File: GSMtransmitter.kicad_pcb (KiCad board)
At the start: 2 copper layers, 69 x 83 mm, 139 parts, among them J1 DS1134-S80BPX, J10 UART1, J11 DG390-5.0-02P, J2 Conn_DEGSON_01x02_Pin, J3 Conn_DEGSON_01x02_Pin, J4 Conn_DEGSON_01x02_Pin, J5 RF Antenna, J6 USB-C, J7 1042240820, J8 1042240820, J9 SWD, Q1 MUN5233DW1, SW1 SM5-180UP-1, U1 AP63203WU, U2 AP63200WU, U3 SIM800C-DS, U4 USBLC6-2SC6, U5 STM32L072CBT6, Y1 4 MHz, Y2 32768 kHz

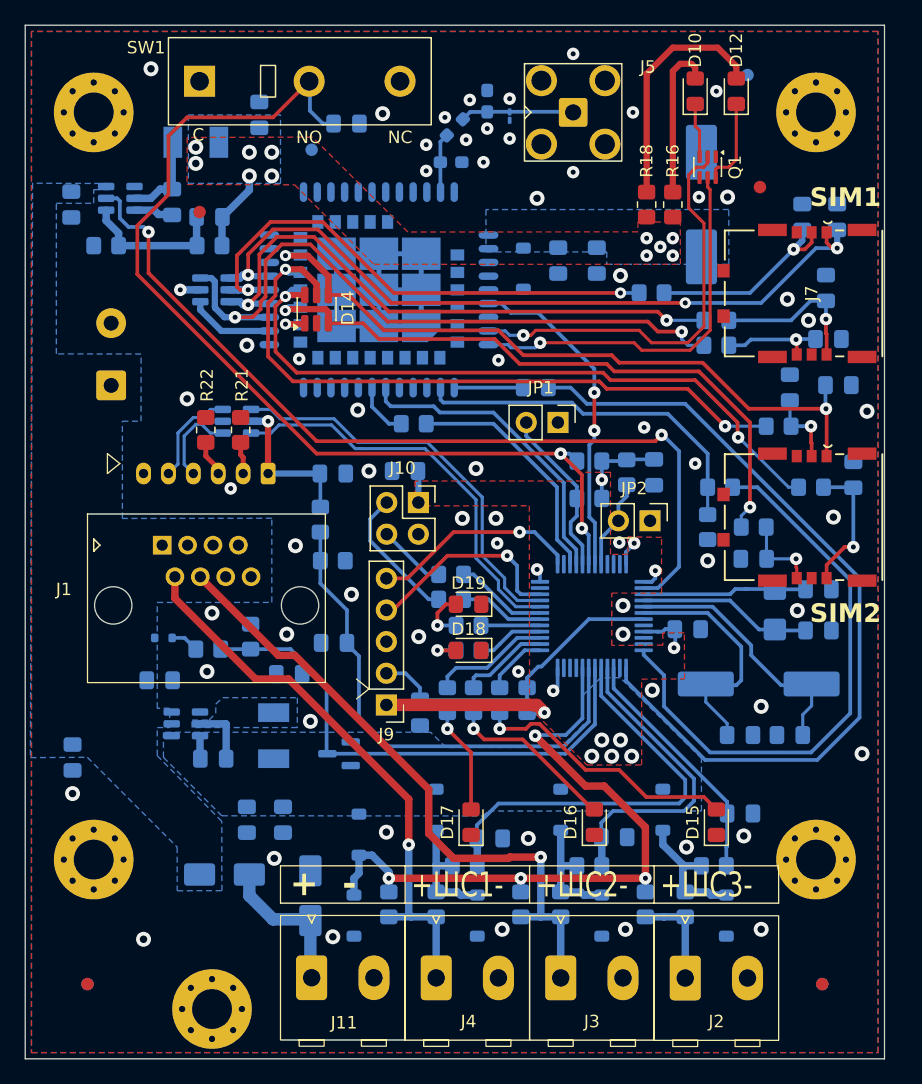
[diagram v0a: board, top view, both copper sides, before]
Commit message: Replace SIM800DC with A7682E
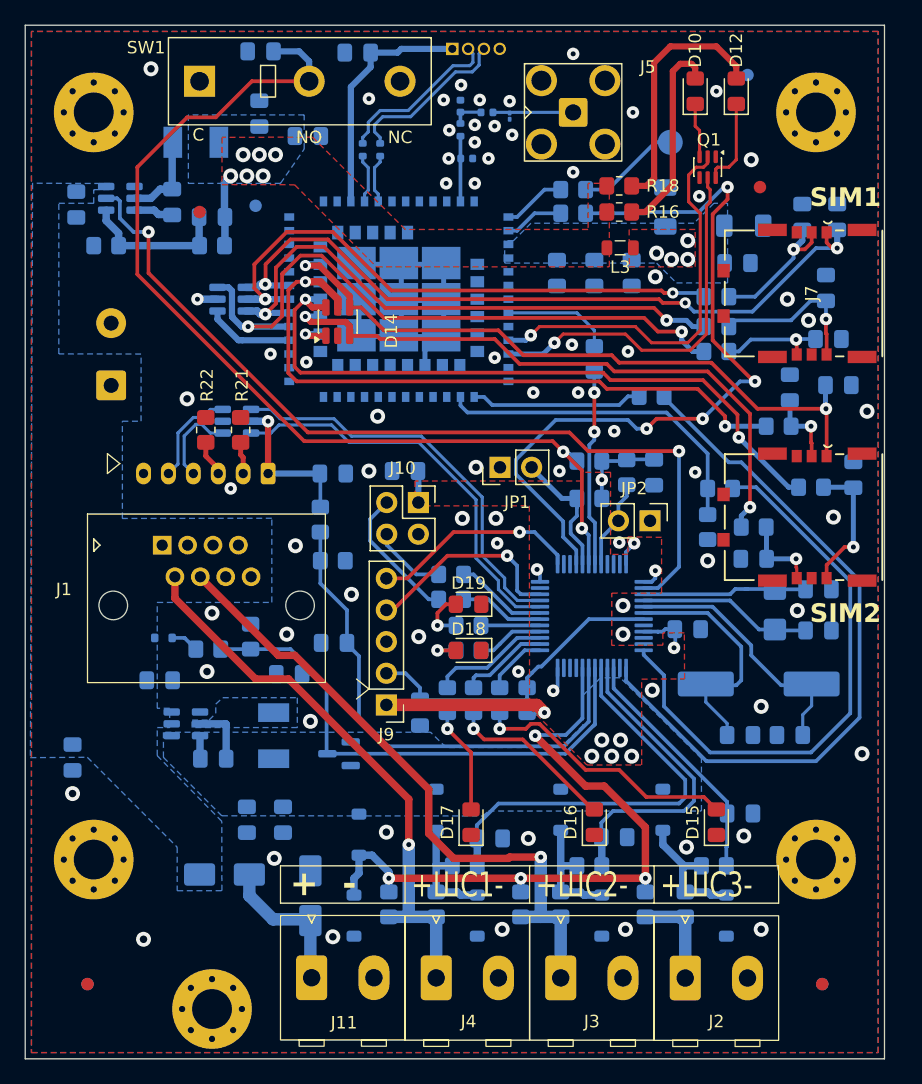
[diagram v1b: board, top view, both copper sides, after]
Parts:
- removed C11: 100nF, Capacitor_SMD:C_0805_2012Metric_Pad1.18x1.45mm_HandSolder
- removed D9: MMSZ5231BT1G, Diode_SMD:D_SOD-123
- removed R14: 1k, Resistor_SMD:R_0805_2012Metric_Pad1.20x1.40mm_HandSolder
- removed U3: SIM800C-DS, footprints:SIMCom_SIM800C-DS
- added C39: 100nF, Capacitor_SMD:C_0805_2012Metric_Pad1.18x1.45mm_HandSolder, B.Cu at (76.7, 42.9)
- added C40: 22uF, Capacitor_SMD:C_0805_2012Metric_Pad1.18x1.45mm_HandSolder, B.Cu at (50.7, 31.9)
- added C41: 1 uF, Capacitor_SMD:C_0805_2012Metric_Pad1.18x1.45mm_HandSolder, B.Cu at (85.2, 42.1)
- added C42: 100 uF, Capacitor_SMD:C_1206_3216Metric_Pad1.33x1.80mm_HandSolder, B.Cu at (85.7, 39.1)
- added C43: 100 uF, Capacitor_SMD:C_1206_3216Metric_Pad1.33x1.80mm_HandSolder, B.Cu at (79.4, 37.6)
- added C44: 100pF, Capacitor_SMD:C_0402_1005Metric, B.Cu at (65.1, 30.0)
- added C45: 100nF, Capacitor_SMD:C_0805_2012Metric_Pad1.18x1.45mm_HandSolder, B.Cu at (54.7, 25.2)
- added J12: USB_RF, Connector_PinHeader_1.27mm:PinHeader_1x04_P1.27mm_Vertical, B.Cu at (62.3, 24.9)
- added L3: BLM21PG300SN1D, Inductor_SMD:L_0805_2012Metric, F.Cu at (75.8, 40.9)
- added R42: 1k, Resistor_SMD:R_0805_2012Metric_Pad1.20x1.40mm_HandSolder, B.Cu at (73.7, 49.8)
- added R43: 1k, Resistor_SMD:R_0805_2012Metric_Pad1.20x1.40mm_HandSolder, B.Cu at (72.0, 38.1)
- added R44: 1k, Resistor_SMD:R_0805_2012Metric_Pad1.20x1.40mm_HandSolder, B.Cu at (72.0, 36.2)
- added R45: 0, Resistor_SMD:R_0402_1005Metric, B.Cu at (56.5, 33.0)
- added R46: 0, Resistor_SMD:R_0402_1005Metric, B.Cu at (55.1, 33.0)
- added TP1: USB_BOOT, TestPoint:TestPoint_Pad_D2.0mm, B.Cu at (79.8, 32.4)
- added U6: A7682E, footprints:SIMCom_A7682E_LGA-85, B.Cu at (58.0, 45.0)
- C12: value 1000uF x 10V -> 22uF; footprint Capacitor_SMD:CP_Elec_10x10.5 -> Capacitor_SMD:C_0805_2012Metric_Pad1.18x1.45mm_HandSolder
- C15, C16: footprint Capacitor_SMD:C_0603_1608Metric_Pad1.08x0.95mm_HandSolder -> Capacitor_SMD:C_0402_1005Metric
- D11: footprint Diode_SMD:D_01005_0402Metric_Pad0.57x0.30mm_HandSolder -> Diode_SMD:D_01005_0402Metric
- R17: footprint Resistor_SMD:R_0603_1608Metric_Pad0.98x0.95mm_HandSolder -> Resistor_SMD:R_0402_1005Metric
- moved C12 36.2 mm to (46.8, 30.1), turned to -90 degrees
- moved R15 9.33 mm to (78.3, 52.8)
- moved C35 9.01 mm to (46.9, 25.1), turned to 0 degrees
- moved FID6 6.36 mm to (46.5, 37.5)
- moved JP1 5.88 mm to (66.1, 58.5), turned to 90 degrees
- moved R25 5.21 mm to (83.5, 44.8)
- moved R16 4.34 mm to (75.7, 38.0), turned to 0 degrees
- moved R18 2.66 mm to (75.7, 35.9), turned to 0 degrees
- moved C16 2.19 mm to (63.0, 29.5)
- moved D14 1.97 mm to (53.1, 46.8)
- moved D13 1.57 mm to (44.6, 45.0)
- moved C15 1.29 mm to (63.5, 33.7)
- moved C14 1.02 mm to (73.7, 42.9)
- moved C13 1.00 mm to (70.7, 42.9)
- moved R23 0.50 mm to (83.5, 49.2)
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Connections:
- C12 pad 1: +4V -> GNDD
- C12 pad 2: GNDD -> +4V
- C13 pad 2: +4V -> /RFmodule/VBAT
- C14 pad 2: +4V -> /RFmodule/VBAT
- C16 pad 2: Net-(D11-A2) -> Net-(C16-Pad2)
- R17 pad 2: Net-(D11-A2) -> Net-(C16-Pad2)
- U5 pad 39: /UART2_RI -> unconnected-(U5-PB3-Pad39)
- U5 pad 40: /UART2_DTR -> /~{RF_RESET}
- U5 pad 43: /RF_ENABLE -> /~{RF_ENABLE}
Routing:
- net /~{RF_RESET}: track 0.00 -> 62.8 mm, vias 0 -> 4
- net /RF_ENABLE: track 26.7 -> 0.00 mm, vias 2 -> 0
- net /UART2_DTR: track 25.1 -> 0.00 mm
- net /RFmodule/USB_VBUS: track 0.00 -> 19.3 mm
- net /UART2_RI: track 19.2 -> 0.00 mm
- net /~{RF_ENABLE}: track 0.00 -> 15.8 mm, vias 0 -> 2
- net /RFmodule/RF_USB_N: track 0.00 -> 13.5 mm
- net /RFmodule/RF_USB_P: track 0.00 -> 13.5 mm
- net /UART2_RX: track 66.5 -> 56.7 mm
- net Net-(U6-~{PWRKEY}): track 0.00 -> 8.78 mm
- net /RFmodule/BOOT: track 0.00 -> 8.37 mm
- net Net-(U6-UART1_TXD): track 5.59 -> 13.8 mm
- net Net-(U6-BOOT_CFG): track 0.00 -> 5.11 mm
- net Net-(U6-~{RESET}): track 0.00 -> 4.78 mm
- net /SIMcard1/CARD_RST: track 16.3 -> 11.6 mm
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- added copper zone on B.Cu, net /RFmodule/VBAT
- added copper zone on F.Cu, net /RFmodule/VBAT

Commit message: RF 45 degrees
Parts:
- moved TP1 0.80 mm to (80.6, 32.4)
- moved R17 0.60 mm to (63.0, 32.0)
- moved C16 0.50 mm to (63.0, 30.0), turned to -45 degrees
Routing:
- net GNDD: track 42.4 -> 8.08 mm, vias 72 -> 77
- net /RFmodule/BOOT: track 8.37 -> 9.17 mm
